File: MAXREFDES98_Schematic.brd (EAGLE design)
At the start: 72.8 x 25.5 mm, 34 parts, among them U1 MB110S-TP, U2 MB110S-TP, U3 MAX5969AETB+

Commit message: minor changes
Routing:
- net PG_EN/SS_INH: track 13.0 -> 14.7 mm
- net GND: track 105.4 -> 106.2 mm
- net IND_IN: track 34.6 -> 35.3 mm

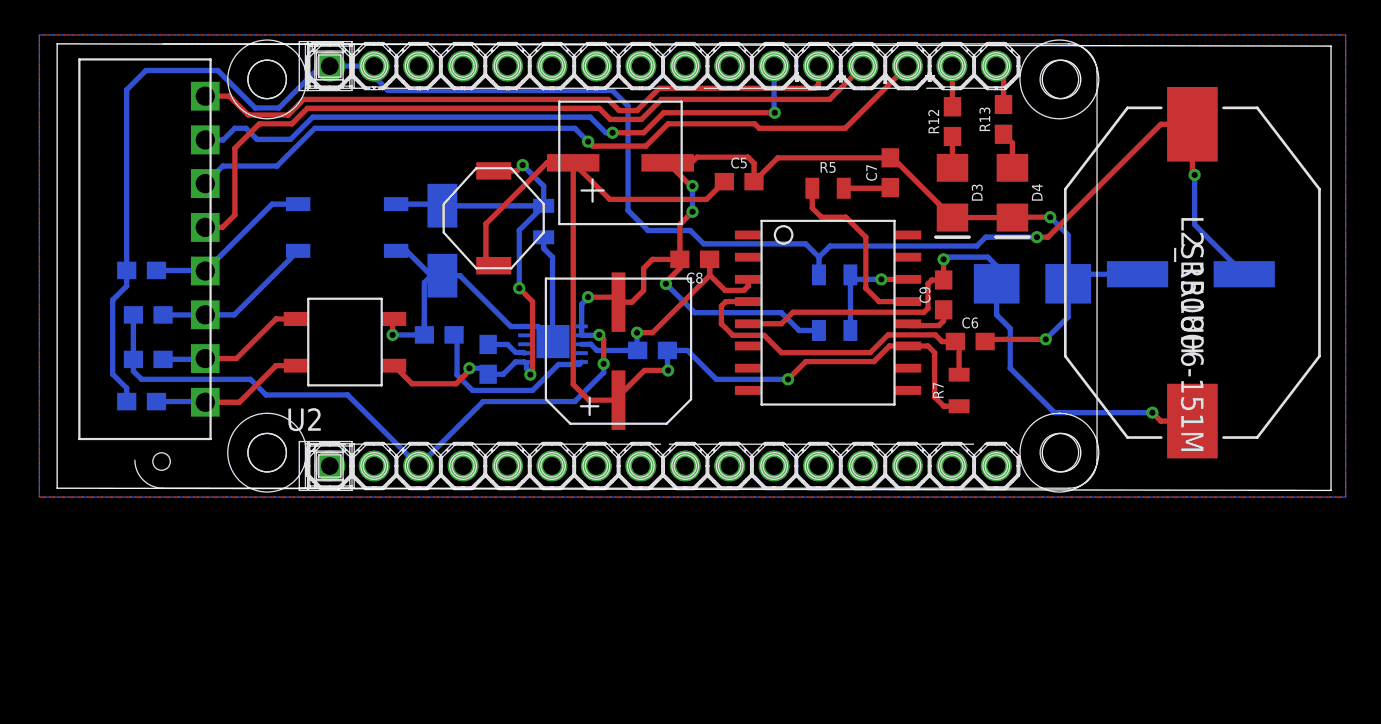
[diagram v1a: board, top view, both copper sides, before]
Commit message: 5V_out line changed
also flipped soething to the back along with wire thickness changed
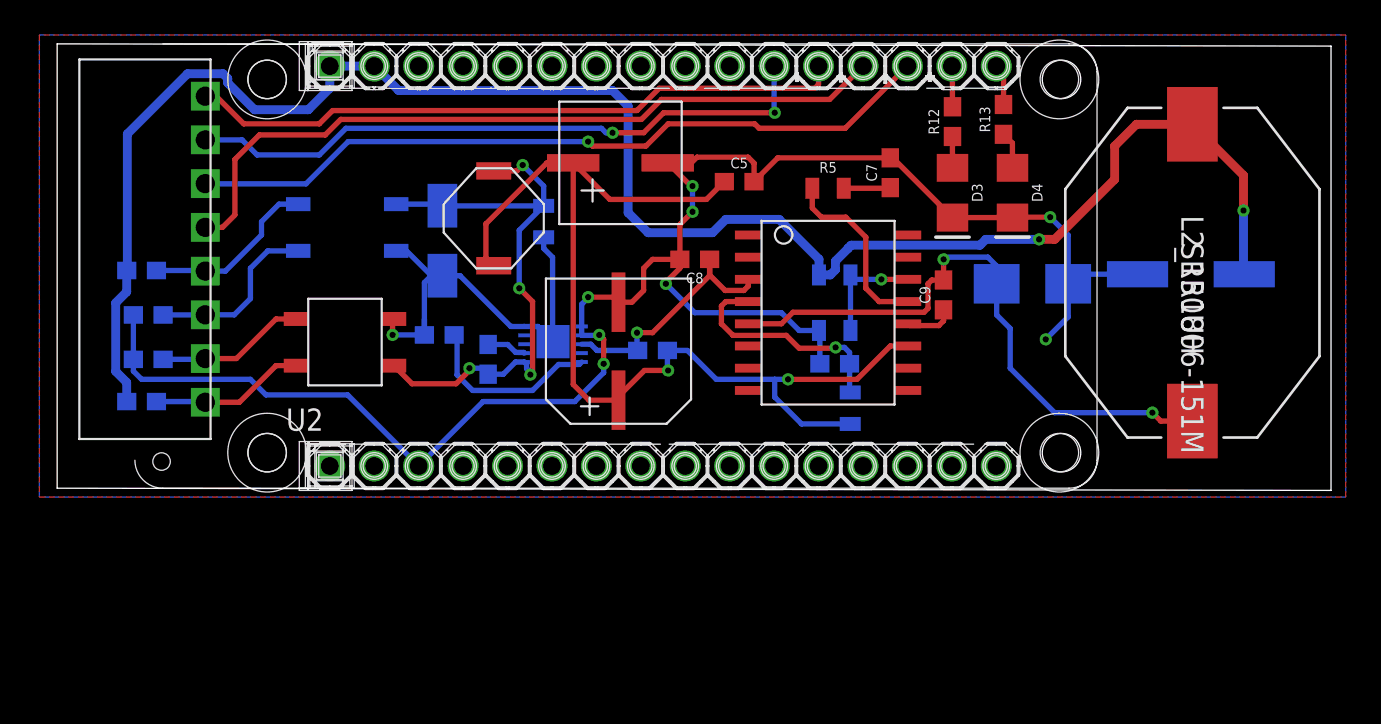
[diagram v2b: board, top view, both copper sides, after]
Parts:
- moved C6 7.85 mm to (44.5, 7.11), flipped to the bottom
- moved R7 6.31 mm to (45.3, 4.57), flipped to the bottom
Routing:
- net OSC: track 19.3 -> 13.0 mm, vias 0 -> 1
- net GND: track 106.2 -> 104.6 mm
- net 5V_OUT: track 104.1 -> 105.4 mm
- net RECT1_IN_MINUS: track 9.24 -> 10.3 mm
- net TD-: track 44.2 -> 43.3 mm
- net TD+: track 44.0 -> 43.3 mm

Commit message: re-route ethernet. clean up a few things
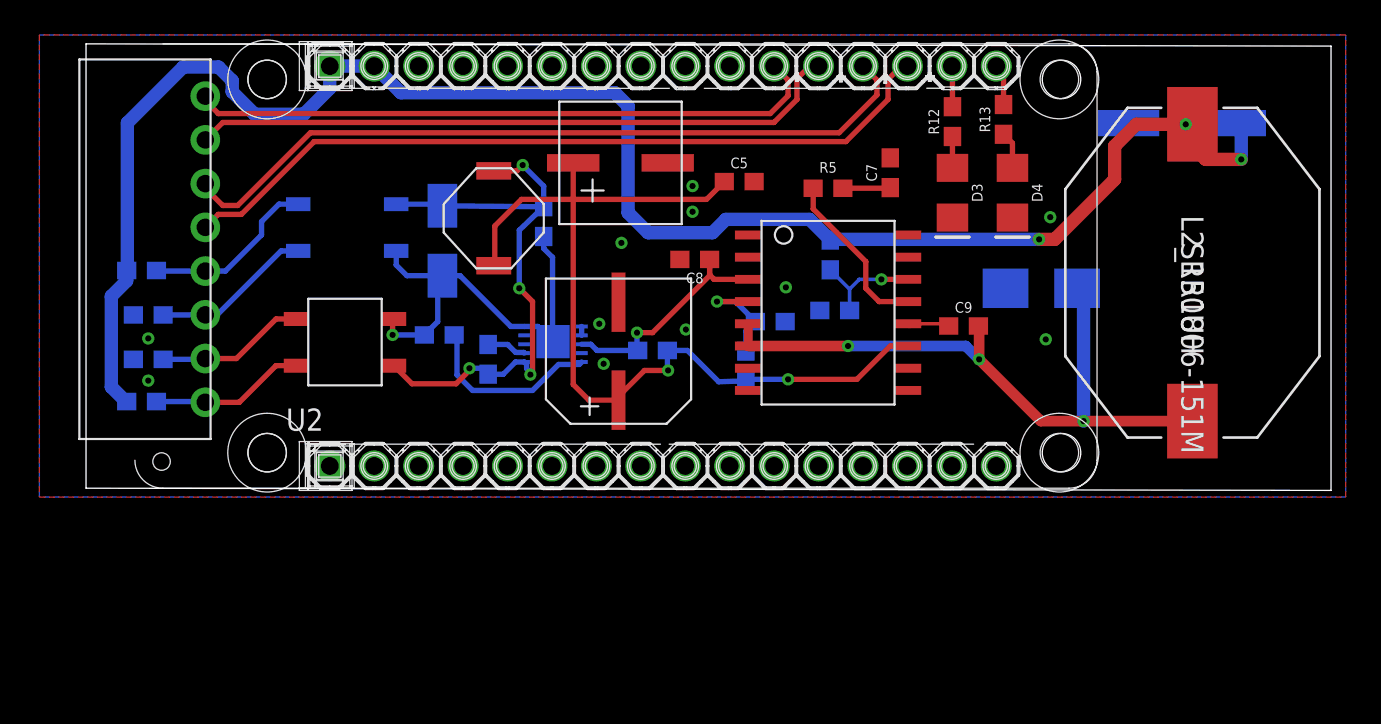
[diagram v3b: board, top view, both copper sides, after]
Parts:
- C1: device SparkFun-Capacitors:0805 -> SparkFun-Capacitors:0603
- CONN: value TERM_BLOCK_PLUG_8POS_STR_2.5MM -> PXC-8-RA-1778683; device Camera_Board_Parts_09_30_2020:TERM_BLOCK_PLUG_8POS_STR_2.5MM -> Phoenix Contact PTSM 8 pin:PXC-8-RA-1778683
- R4, R5, R6, R7: device SparkFun-Resistors:0805 -> SparkFun-Resistors:0603
- moved C3 8.65 mm to (64.6, 21.2)
- moved R7 6.44 mm to (39.4, 6.99)
- moved C6 4.40 mm to (40.8, 9.53), turned to 180 degrees
- moved C9 2.11 mm to (51.8, 9.27), turned to 0 degrees
- moved R4 1.17 mm to (44.2, 13.3), turned to 90 degrees
- moved R6 1.14 mm to (44.5, 10.2)
- moved D2 0.57 mm to (56.3, 11.4), turned to 0 degrees
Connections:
- removed net RD+: CONN.1, U$2.RD+
- removed net RD-: CONN.2, U$2.RD-
- removed net TD+: CONN.3, U$2.TD+
- removed net TD-: CONN.4, U$2.TD-
- new net RD_N: CONN.1, U$2.RD-
- new net RD_P: CONN.2, U$2.RD+
- new net TD_N: CONN.3, U$2.TD-
- new net TD_P: CONN.4, U$2.TD+
- net IND_IN: now also U$1.6
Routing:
- net GND: track 104.6 -> 0.51 mm, vias 8 -> 11
- net TD_P: track 0.00 -> 44.6 mm
- net TD_N: track 0.00 -> 43.7 mm
- net TD+: track 43.3 -> 0.00 mm, vias 1 -> 0
- net TD-: track 43.3 -> 0.00 mm
- net RD+: track 37.7 -> 0.00 mm
- net RD_P: track 0.00 -> 37.5 mm
- net RD-: track 36.8 -> 0.00 mm, vias 2 -> 0
- net RD_N: track 0.00 -> 36.3 mm
- net VDD_L: track 60.6 -> 52.2 mm
- net OSC: track 13.0 -> 6.38 mm
- net IND_IN: track 35.3 -> 38.1 mm, vias 2 -> 3
- net RECT1_IN_MINUS: track 10.3 -> 9.24 mm
- net COMP: track 10.5 -> 9.68 mm
- net 5V_OUT: track 105.4 -> 104.5 mm, vias 2 -> 3
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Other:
- board size 72.8 x 25.5 mm -> 71.2 x 25.5 mm

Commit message: Added GND to Buck and changed some wire widths.
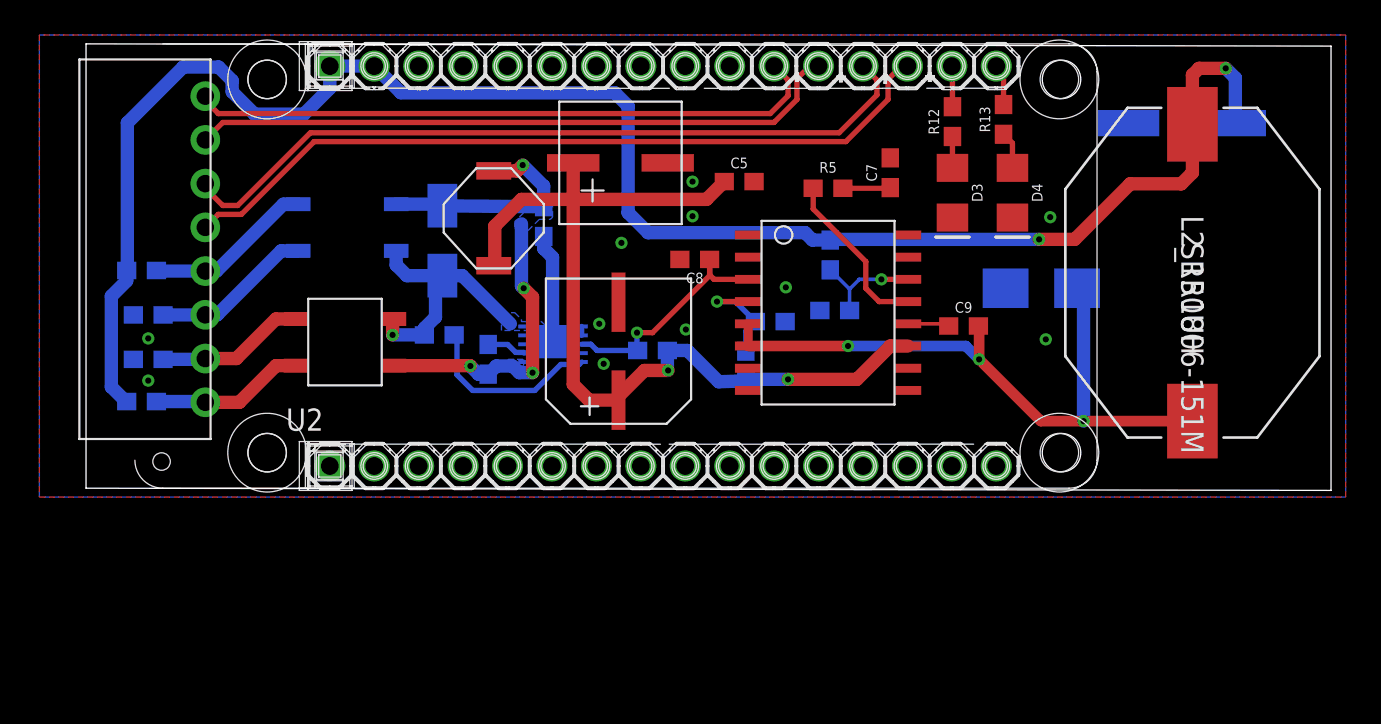
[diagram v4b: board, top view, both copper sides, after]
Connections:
- net GND: now also U$1.2
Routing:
- net VDD: track 33.3 -> 30.4 mm
- net VSS_EP: track 24.3 -> 21.4 mm
- net 5V_OUT: track 104.5 -> 102.6 mm, vias 3 -> 2
- added copper zone on layer 16, net VDD
- added copper zone on layer 16, net VSS_EP

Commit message: Deleted PoE and added Transformer
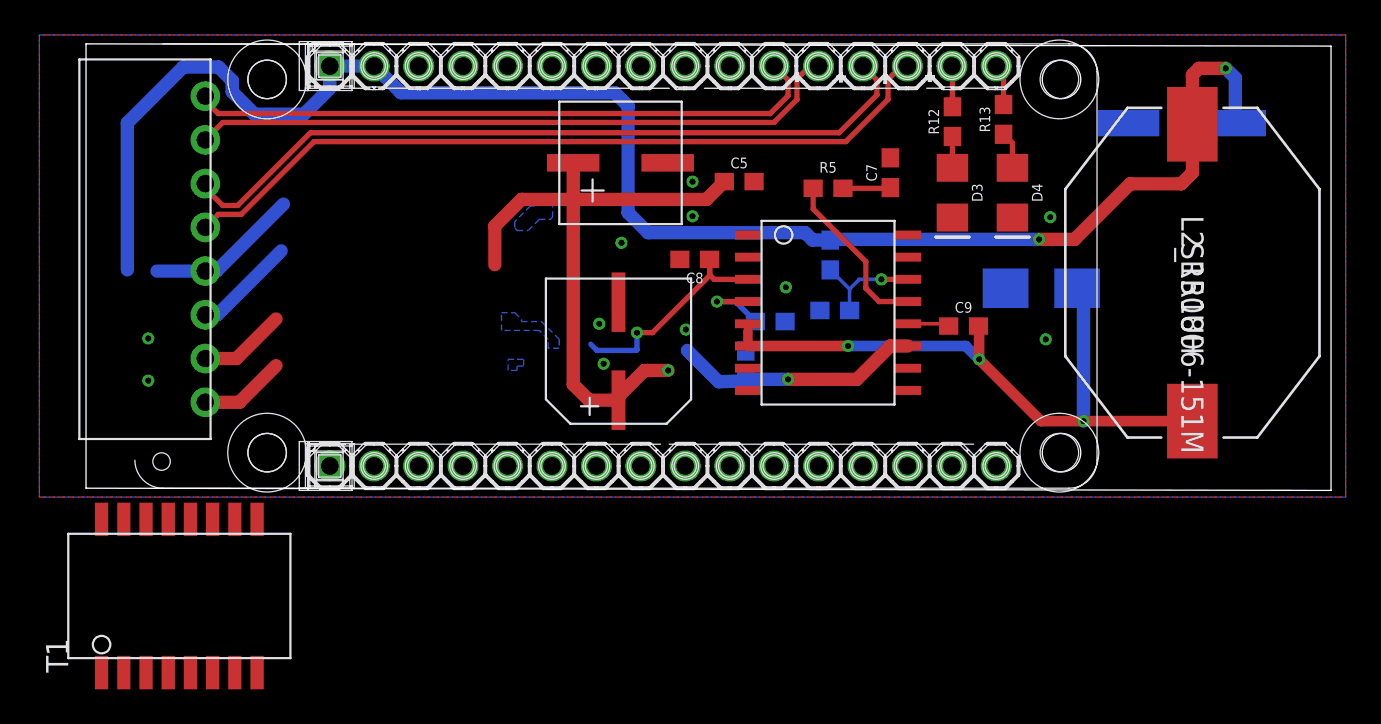
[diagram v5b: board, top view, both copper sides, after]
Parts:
- removed C1: 0.1uF, SparkFun-Capacitors:0603
- removed D1: SMAJ58A-13-F, SMAJ58A-13-F:SMAJ58A-13-F
- removed L1: SD53-3R3-R, SD53-3R3-R:SD53-3R3-R
- removed R1: 619, SparkFun-Resistors:0603
- removed R10, R11, R8, R9: 0, SparkFun-Resistors:0603
- removed R2: 24.9k, SparkFun-Resistors:0603
- removed R3: 3.3M, SparkFun-Resistors:0603
- removed U1, U2: MB110S-TP, MB110S-TP:MB110S-TP
- removed U3: MAX5969AETB+, MAX5969AETB+_Library:MAX5969AETB+
- added T1: TG110-S055N2RL, CameraBoard_Library:TG110-S055N2RL
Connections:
- removed net CLS: R1.2, U3.10
- removed net DET: R2.1, U3.2
- removed net VDD: C1.1, D1.P$1, L1.P$1, R2.2, U1.+, U2.+, U3.1
- removed net VSS_EP: C1.2, D1.P$2, R1.1, U1.-, U2.-, U3.5, U3.EP
- new net ETH_TD0_BP_N: T1.6
- new net ETH_TD0_BP_P: T1.8
- new net ETH_TD0_N: T1.11
- new net ETH_TD0_P: T1.9
- new net ETH_TD1_BP_N: T1.1
- new net ETH_TD1_BP_P: T1.3
- new net ETH_TD1_N: T1.16
- new net ETH_TD1_P: T1.14
- new net N$11: T1.2
- new net N$14: T1.7
- new net N$4: T1.10
- new net N$5: T1.15
- net 5V_OUT: no longer R11.1, R8.1
- net GND: no longer R10.1, R9.1, U3.6, U3.7
- net PG_EN/SS_INH: no longer R3.1, U3.8
- net RECT1_IN_MINUS: no longer R10.2, U1.~1
- net RECT1_IN_PLUS: no longer R8.2, U1.~2
- net RECT2_IN_MINUS: no longer R9.2, U2.~1
- net RECT2_IN_PLUS: no longer R11.2, U2.~2
- net VDD_L: no longer L1.P$2, R3.2
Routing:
- net VDD: track 30.4 -> 0.00 mm, vias 4 -> 0
- net VSS_EP: track 21.4 -> 0.00 mm, vias 1 -> 0
- net CLS: track 10.5 -> 0.00 mm
- net 5V_OUT: track 102.6 -> 94.3 mm
- net RECT2_IN_PLUS: track 8.86 -> 4.97 mm
- net RECT2_IN_MINUS: track 8.55 -> 5.04 mm
- net RECT1_IN_MINUS: track 9.24 -> 5.86 mm
- net VDD_L: track 52.2 -> 49.9 mm
- net DET: track 2.28 -> 0.00 mm
- net RECT1_IN_PLUS: track 9.70 -> 8.81 mm
- net PG_EN/SS_INH: track 14.0 -> 13.4 mm
- net GND: track 0.51 -> 0.00 mm

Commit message: Updated board with transformer circuit and new connector signals
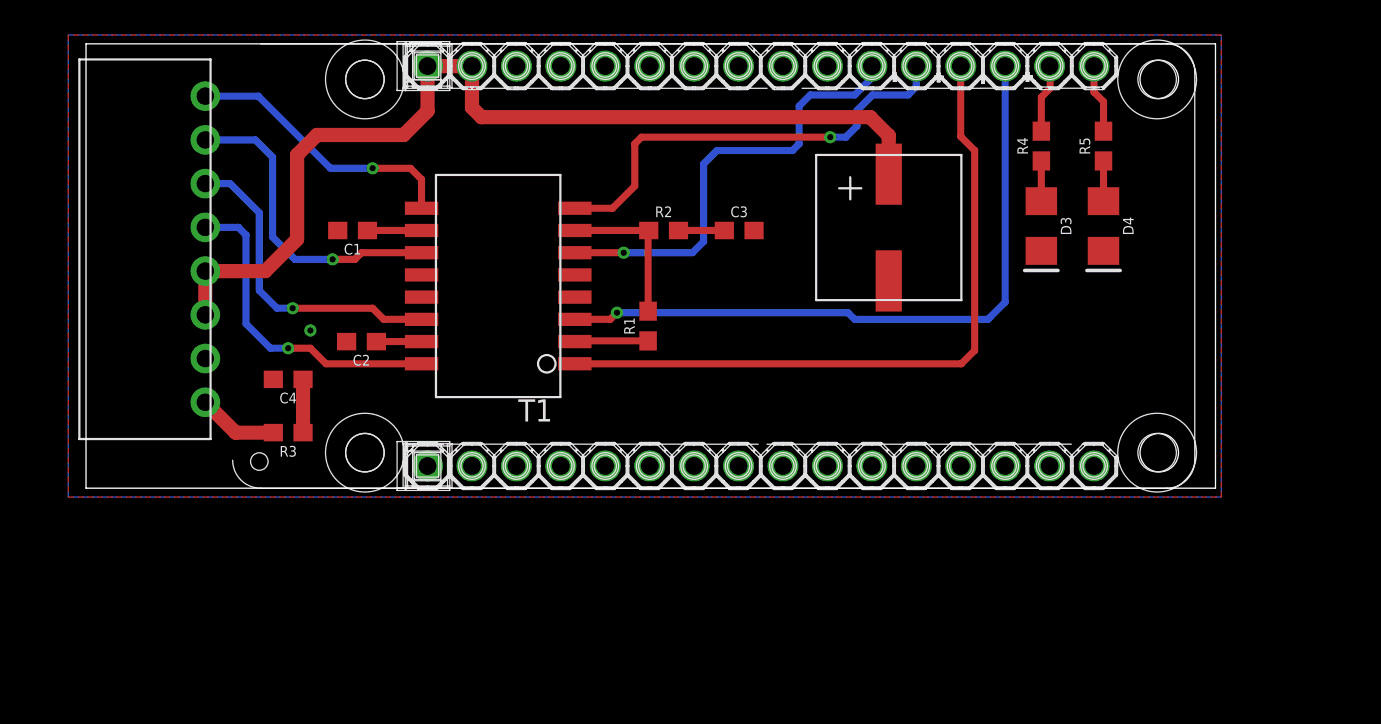
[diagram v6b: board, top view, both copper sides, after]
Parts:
- removed C6: 2.7nF, SparkFun-Capacitors:0603
- removed C7: 22nF, SparkFun-Capacitors:0603
- removed C8, C9: 100nF, SparkFun-Capacitors:0603
- removed D2: STPS3L60USMB_STM-M, Camera_Board_Parts_09_30_2020:SMB_STM-M
- removed L2_150UH: SRR1806-151M, CameraBoard_Library:IND_BOURNS_SRR1806
- removed R12, R13: 470, SparkFun-Resistors:0603
- removed R6: 4.7k, SparkFun-Resistors:0603
- removed R7: 20k, SparkFun-Resistors:0603
- removed U$1: L4978D013TR, Camera_Board_Parts_09_30_2020:L4978D013TR
- added C1: 0.1uF, SparkFun-Capacitors:0603
- added R1, R2: 75, SparkFun-Resistors:0603
- added R3: 0, SparkFun-Resistors:0603
- C2: value EEE-1JA220UP -> 0.1uF; device EEE-1JA220UP:EEE-1JA220UP -> SparkFun-Capacitors:0603
- C3: value 337AXZ025M -> 1nF; device CameraBoard_Library:337AXZ025M -> SparkFun-Capacitors:0603
- C4: value EXV227M016A9HAA -> 0nF; device CameraBoard_Library:EXV227M016A9HAA -> SparkFun-Capacitors:0603
- C5: value 220nF -> 337AXZ025M; device SparkFun-Capacitors:0603 -> CameraBoard_Library:337AXZ025M
- R4: value 2.7k -> 470
- R5: value 9.1k -> 470
- moved T1 33.0 mm to (29.6, 5.21), turned to 90 degrees
- moved C3 26.5 mm to (39.0, 14.7), flipped to the top, turned to 0 degrees
- moved C4 22.2 mm to (13.2, 6.22), turned to 180 degrees
- moved R5 15.9 mm to (59.8, 19.6), turned to 90 degrees
- moved R4 13.6 mm to (56.3, 19.6), flipped to the top
- moved C2 11.5 mm to (17.4, 8.38), turned to 180 degrees
- moved C5 9.18 mm to (47.9, 15.2), turned to 180 degrees
- moved U$2 5.59 mm to (10.0, 25.4)
- moved D4 5.54 mm to (59.8, 15.0)
- moved D3 5.43 mm to (56.3, 15.0)
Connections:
- removed net 3V3: U$2.3V3
- removed net BOOT: C9.1, U$1.12
- removed net COMP: R5.1, U$1.13
- removed net ETH_TD0_BP_N: T1.6
- removed net ETH_TD0_BP_P: T1.8
- removed net ETH_TD0_N: T1.11
- removed net ETH_TD0_P: T1.9
- removed net ETH_TD1_BP_N: T1.1
- removed net ETH_TD1_BP_P: T1.3
- removed net ETH_TD1_N: T1.16
- removed net ETH_TD1_P: T1.14
- removed net FB: R4.1, R6.2, U$1.14
- removed net IND_IN: C9.2, D2.1, L2_150UH.2, U$1.5, U$1.6
- removed net N$5: T1.15
- removed net N$6: C7.1, R5.2
- removed net OSC: C6.1, R7.2, U$1.4
- removed net PG_EN/SS_INH: C8.1, U$1.3
- removed net RECT1_IN_MINUS: CONN.6
- removed net RECT1_IN_PLUS: CONN.5
- removed net RECT2_IN_MINUS: CONN.7
- removed net RECT2_IN_PLUS: CONN.8
- removed net VDD_L: C2.PLUS, C4.PLUS, C5.1, R7.1, U$1.11
- new net ETH_RD_N: T1.6, U$2.RD-
- new net ETH_RD_P: T1.8, U$2.RD+
- new net ETH_TD0_GND: C1.1, T1.10
- new net ETH_TD1_GND: C2.1, T1.15
- new net ETH_TD_N: T1.1, U$2.TD-
- new net ETH_TD_P: T1.3, U$2.TD+
- new net N$3: C3.1, R2.2
- new net SHIELD: CONN.8, R3.2
- net 5V_OUT: now also C5.PLUS, CONN.5, CONN.6; no longer C3.PLUS, L2_150UH.1, R4.2
- net GND: now also C1.2, C2.2, C3.2, C4.2, C5.MINUS, CONN.7; no longer C2.MINUS, C3.MINUS, C4.MINUS, C5.2, C6.2, C7.2, C8.2, D2.2, R6.1, U$1.2
- net LNK: now also R4.2; no longer R12.2
- net N$1: now also R4.1; no longer R12.1
- net N$11: now also R1.1
- net N$14: now also R1.2, R2.1
- net N$2: now also R5.1; no longer R13.1
- net N$4: now also C4.1, R3.1; no longer T1.10
- net RD_N: now also CONN.2, T1.11; no longer CONN.1, U$2.RD-
- net RD_P: now also CONN.1, T1.9; no longer CONN.2, U$2.RD+
- net SPD: now also R5.2; no longer R13.2
- net TD_N: now also CONN.4, T1.16; no longer CONN.3, U$2.TD-
- net TD_P: now also CONN.3, T1.14; no longer CONN.4, U$2.TD+
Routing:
- net VDD_L: track 49.9 -> 0.00 mm, vias 2 -> 0
- net ETH_TD_N: track 0.00 -> 39.8 mm
- net ETH_TD_P: track 0.00 -> 38.8 mm, vias 0 -> 1
- net 5V_OUT: track 94.3 -> 56.0 mm, vias 2 -> 0
- net IND_IN: track 38.1 -> 0.00 mm, vias 3 -> 0
- net TD_P: track 44.6 -> 18.2 mm, vias 0 -> 1
- net ETH_RD_N: track 0.00 -> 25.7 mm, vias 0 -> 1
- net ETH_RD_P: track 0.00 -> 25.5 mm, vias 0 -> 1
- net TD_N: track 43.7 -> 18.6 mm, vias 0 -> 1
- net RD_P: track 37.5 -> 16.0 mm, vias 0 -> 1
- net RD_N: track 36.3 -> 18.0 mm, vias 0 -> 1
- net PG_EN/SS_INH: track 13.4 -> 0.00 mm, vias 1 -> 0
- net COMP: track 9.68 -> 0.00 mm
- net N$14: track 0.00 -> 8.86 mm
- net RECT1_IN_PLUS: track 8.81 -> 0.00 mm
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- removed copper zone on layer 16, net VDD
- removed copper zone on layer 16, net VSS_EP
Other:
- board size 71.2 x 25.5 mm -> 64.6 x 25.4 mm
